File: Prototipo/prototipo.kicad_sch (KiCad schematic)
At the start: 18 parts, among them J1 Conn_02x12_Odd_Even

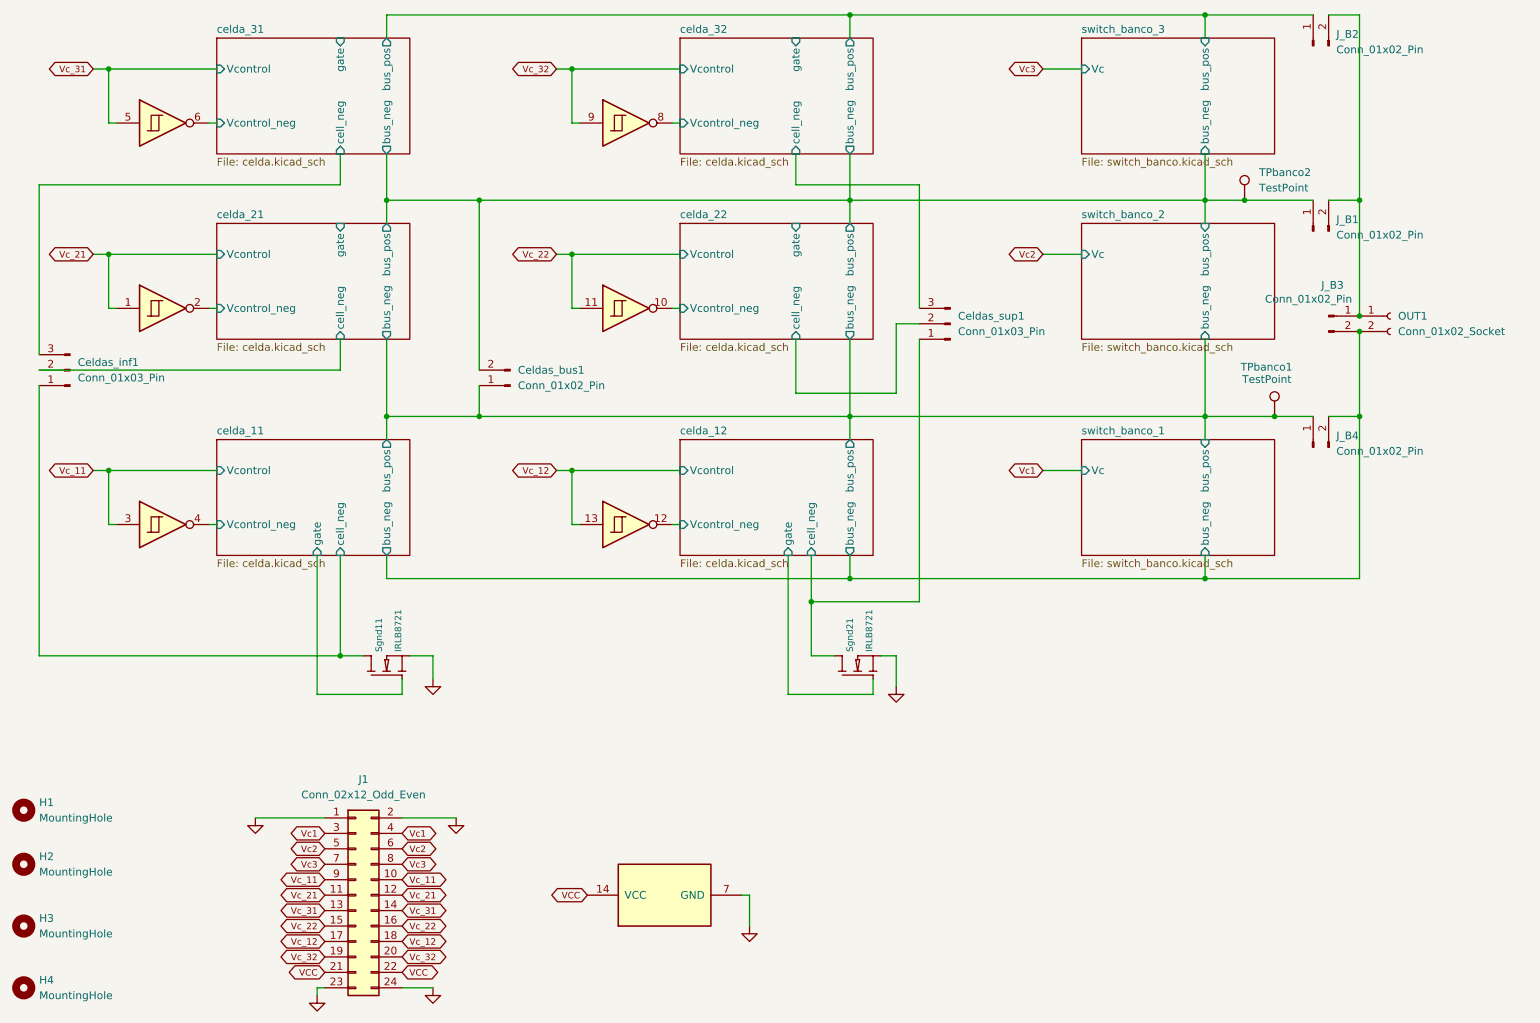
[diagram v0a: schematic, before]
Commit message: se suman los leds al pcb
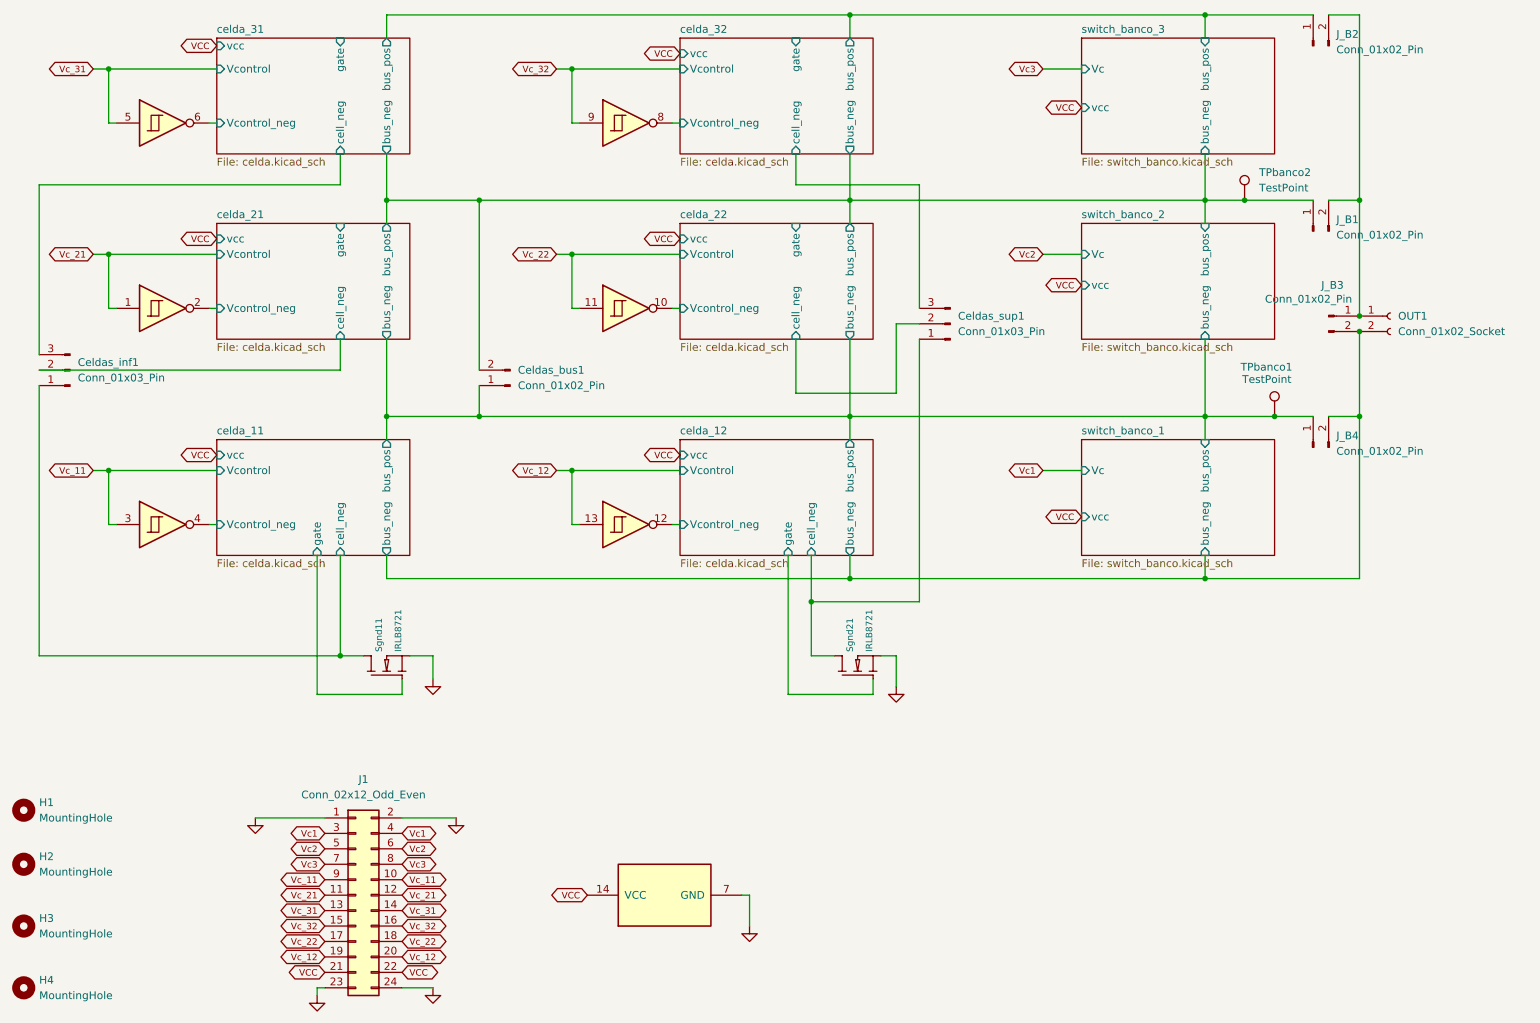
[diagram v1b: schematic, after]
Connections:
- net Vc_12: now also J1.19 (Pin_19), J1.20 (Pin_20); no longer J1.17 (Pin_17), J1.18 (Pin_18)
- net Vc_22: now also J1.17 (Pin_17), J1.18 (Pin_18); no longer J1.15 (Pin_15), J1.16 (Pin_16)
- net Vc_32: now also J1.15 (Pin_15), J1.16 (Pin_16); no longer J1.19 (Pin_19), J1.20 (Pin_20)
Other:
- sheet celda_11 ports: added vcc; removed none
- sheet celda_12 ports: added vcc; removed none
- sheet celda_21 ports: added vcc; removed none
- sheet celda_22 ports: added vcc; removed none
- sheet celda_31 ports: added vcc; removed none
- sheet celda_32 ports: added vcc; removed none
- sheet switch_banco_1 ports: added vcc; removed none
- sheet switch_banco_2 ports: added vcc; removed none
- sheet switch_banco_3 ports: added vcc; removed none
